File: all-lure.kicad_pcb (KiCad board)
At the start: 4 copper layers, 110 x 114 mm, 95 parts, among them J1 XDP, J2 mSATA, J3 mPCIe, J4 HSE, J5 Conn_01x02, J6 GPIO, J8 0480995701, J9 0480995701, U1 SC189HSKTRT, U2 SC189ZSKTRT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

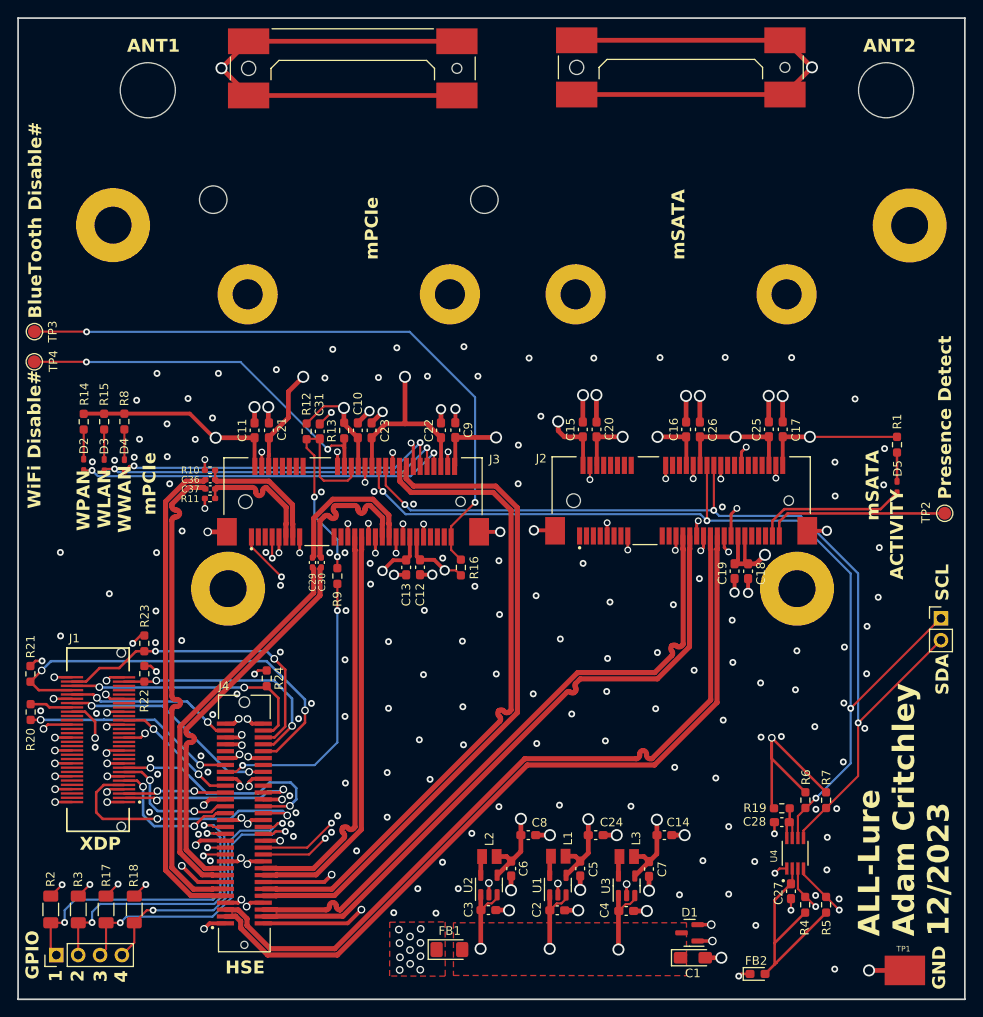
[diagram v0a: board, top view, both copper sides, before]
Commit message: fact(pcb): change trace width for 3313 fabrication. meander jtag traces. fix broken ground plane under pci ref clock.
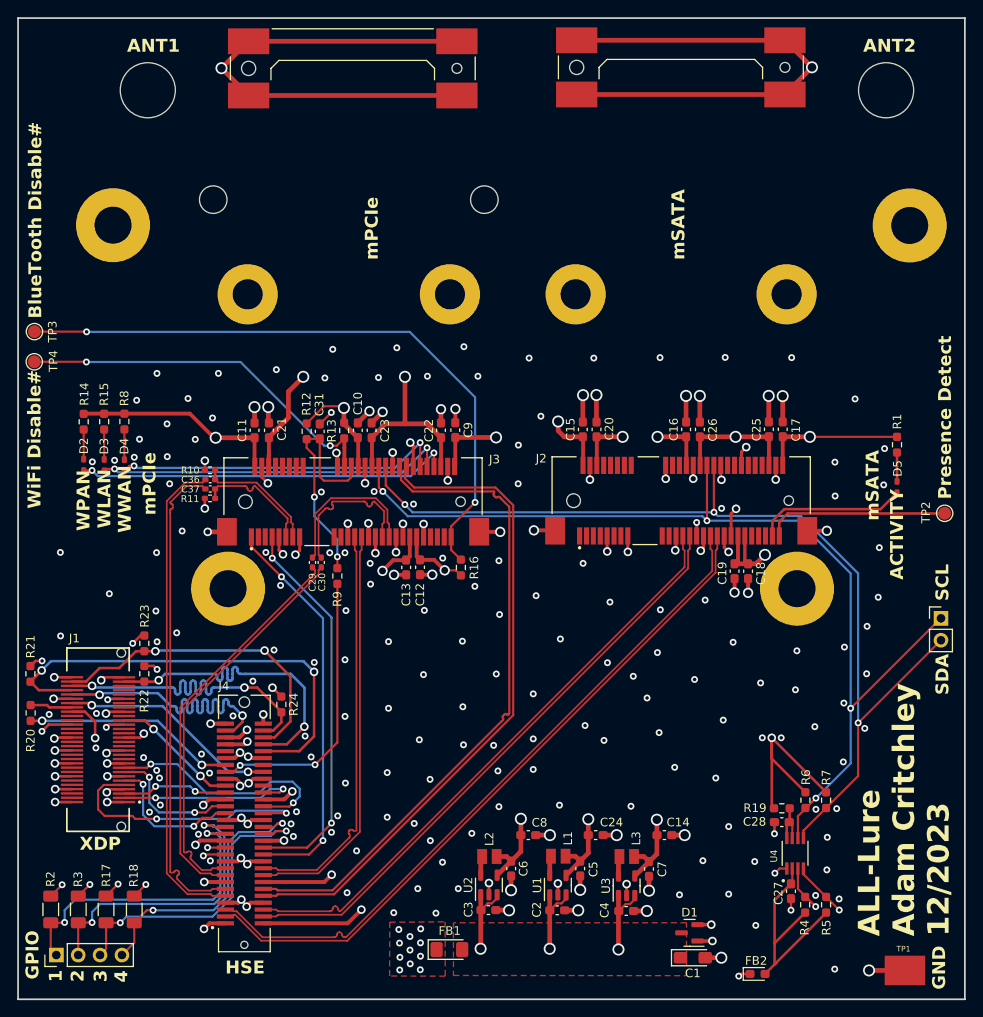
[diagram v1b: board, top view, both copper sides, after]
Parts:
- moved R24 3.48 mm to (118.6, 121.6)
- moved R20 0.11 mm to (89.5, 122.6)
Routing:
- net /TDO: track 19.6 -> 37.0 mm
- net /mSATA_TX_P: track 91.0 -> 80.3 mm
- net /mSATA_TX_N: track 90.9 -> 80.3 mm
- net /TCK: track 27.9 -> 37.2 mm
- net /TDI: track 29.7 -> 38.3 mm
- net /mSATA_RX_P: track 76.0 -> 70.0 mm
- net /mSATA_RX_N: track 76.0 -> 69.9 mm
- net /nTRST: track 48.9 -> 53.8 mm
- net /VP18S: track 24.4 -> 25.9 mm
- net /OBSDATA_A3: track 27.5 -> 28.6 mm
- net /REFCLK_P: track 15.1 -> 14.1 mm
- net /OBSDATA_A0: track 31.9 -> 31.0 mm
- net /REFCLK_N: track 15.0 -> 14.1 mm
- net /PETN: track 17.5 -> 18.1 mm
- net /PETP: track 17.6 -> 18.2 mm
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- added copper zone on In2.Cu, net GND

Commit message: feat(pcb): update with latest attempt at mSATA and mPCIE
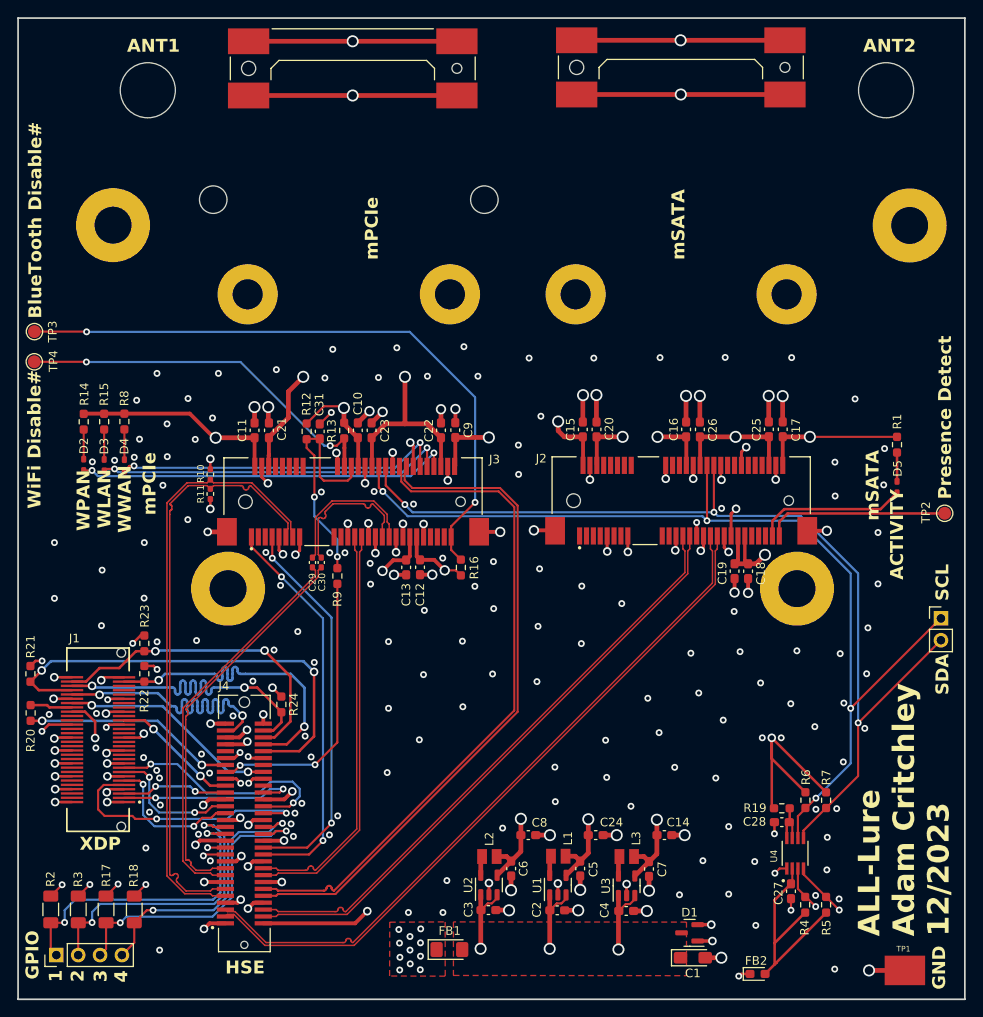
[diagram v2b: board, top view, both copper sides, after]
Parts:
- removed C36, C37: 0.1uF 16V, Capacitor_SMD:C_0402_1005Metric_Pad0.74x0.62mm_HandSolder
- moved R11 0.52 mm to (110.3, 97.2), turned to -90 degrees
- moved R10 0.50 mm to (110.3, 94.9), turned to 90 degrees
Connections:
- J4 pad 11: /mPCIe_REFCLK_N -> /REFCLK_N
- J4 pad 9: /mPCIe_REFCLK_P -> /REFCLK_P
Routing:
- net /mPCIe_REFCLK_P: track 56.7 -> 0.00 mm
- net /mPCIe_REFCLK_N: track 56.6 -> 0.00 mm
- net /REFCLK_P: track 14.1 -> 70.5 mm
- net /REFCLK_N: track 14.1 -> 70.4 mm
- net GND: track 341.5 -> 318.2 mm, vias 265 -> 253
- net /mPCIe_3V3: track 192.7 -> 190.5 mm
- net /mSATA_TX_P: track 80.3 -> 81.6 mm
- net /mSATA_TX_N: track 80.3 -> 81.5 mm
- net /USB_HOST_DN: track 77.4 -> 78.4 mm
- net /USB_HOST_DP: track 77.5 -> 78.4 mm
- net /PETP: track 18.2 -> 17.3 mm
- net /PETN: track 18.1 -> 17.2 mm
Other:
- board text added: "0"
- board text added: "0 mm"
- board text added: "0.015 mm"
- board text added: "0.02"
- board text added: "0.03 mm"
- board text added: "0.035 mm"
- board text added: "0.1270 mm / 0.1270 mm"
- board text added: "0.203 mm"
- board text added: "0.3000 mm"
- board text added: "1.03 mm"
- board text added: "1.5960 mm"
- board text added: "110.0000 mm x 114.0000 mm"
- board text added: "3.3"
- board text added: "4.4"
- board text added: "4.6"
- board text added: "B.Cu"
- board text added: "B.Mask"
- board text added: "B.Paste"
- board text added: "B.Silkscreen"
- board text added: "BOARD CHARACTERISTICS"
- board text added: "Board Thickness:"
- board text added: "Board overall dimensions:"
- board text added: "Bottom Silk Screen"
- board text added: "Bottom Solder Mask"
- board text added: "Bottom Solder Paste"
- board text added: "Castellated pads:"
- board text added: "Color"
- board text added: "Copper Finish:"
- board text added: "Copper Layer Count:"
- board text added: "Dielectric"
- board text added: "Direct Printing"
- board text added: "Edge card connectors:"
- board text added: "Epsilon R"
- board text added: "F.Cu"
- board text added: "F.Mask"
- board text added: "F.Paste"
- board text added: "F.Silkscreen"
- board text added: "FR4"
- board text added: "FR4 natural"
- board text added: "Green"
- board text added: "Impedance Control:"
- board text added: "In1.Cu"
- board text added: "In2.Cu"
- board text added: "JLC041611-7628"
- board text added: "Layer Name"
- board text added: "Liquid Ink"
- board text added: "Loss Tangent"
- board text added: "Material"
- board text added: "Min hole diameter:"
- board text added: "Min track/spacing:"
- board text added: "No"
- board text added: "None"
- board text added: "Plated Board Edge:"
- board text added: "Thickness (mm)"
- board text added: "Top Silk Screen"
- board text added: "Top Solder Mask"
- board text added: "Top Solder Paste"
- board text added: "Type"
- board text added: "White"
- board text added: "Yes"
- board text added: "copper"
- board text added: "core"
- board text added: "prepreg"
